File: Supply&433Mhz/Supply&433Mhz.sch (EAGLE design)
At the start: 15 parts, among them K1 61004021821, P1 DF11-06-2DSA, Q1 BS170

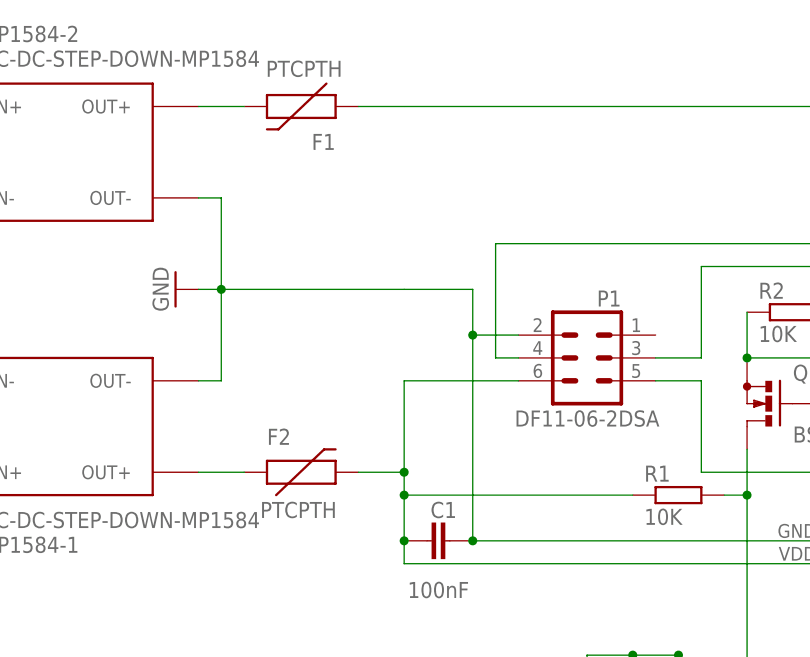
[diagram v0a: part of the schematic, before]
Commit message: Revert "Remove Schottky - Diodes, since already on DC/DC buck converter."
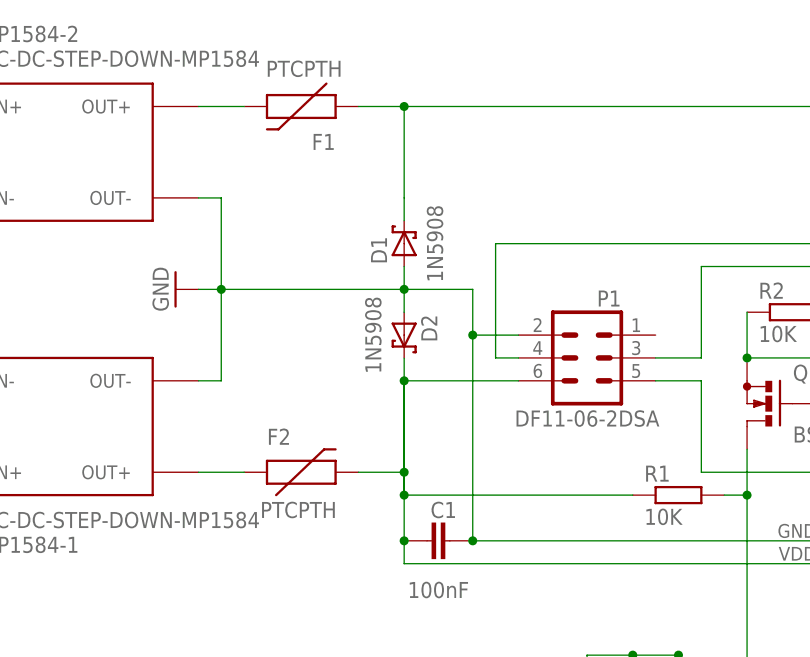
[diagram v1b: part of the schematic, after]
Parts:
- added D1, D2: 1N5908, diode:1N5908
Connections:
- net GND: now also D1.A, D2.A
- net N$2: now also D2.C
- net N$5: now also D1.C
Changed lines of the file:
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@@
 <part name="P1" library="con-hirose-df11" deviceset="DF11-06-2DSA" device=""/>
 <part name="24V" library="con-wuerth" deviceset="691131710002" device=""/>
+<part name="D1" library="diode" deviceset="1N5908" device=""/>
+<part name="D2" library="diode" deviceset="1N5908" device=""/>
 <part name="F1" library="SparkFun-PowerIC" deviceset="PTC" device="PTH"/>
 <part name="F2" library="SparkFun-PowerIC" deviceset="PTC" device="PTH"/>
@@
 </instance>
 <instance part="24V" gate="G$1" x="20.32" y="81.28" rot="MR0"/>
+<instance part="D1" gate="1" x="88.9" y="83.82" smashed="yes" rot="R90">
+<attribute name="NAME" x="86.995" y="81.534" size="1.778" layer="95" rot="R90"/>
+<attribute name="VALUE" x="91.44" y="83.82" size="1.778" layer="96" rot="R90" align="top-center"/>
+</instance>
+<instance part="D2" gate="1" x="88.9" y="73.66" smashed="yes" rot="R270">
+<attribute name="NAME" x="90.805" y="75.946" size="1.778" layer="95" rot="R270"/>
+<attribute name="VALUE" x="86.36" y="73.66" size="1.778" layer="96" rot="R270" align="top-center"/>
+</instance>
 <instance part="F1" gate="G$1" x="78.74" y="99.06" rot="R180"/>
 <instance part="F2" gate="G$1" x="76.2" y="58.42"/>
@@
 <pinref part="GND1" gate="1" pin="GND"/>
 <wire x1="66.04" y1="78.74" x2="68.58" y2="78.74" width="0.1524" layer="91"/>
+<pinref part="D2" gate="1" pin="A"/>
 <wire x1="68.58" y1="78.74" x2="88.9" y2="78.74" width="0.1524" layer="91"/>
+<wire x1="88.9" y1="78.74" x2="88.9" y2="76.2" width="0.1524" layer="91"/>
+<pinref part="D1" gate="1" pin="A"/>
+<wire x1="88.9" y1="78.74" x2="88.9" y2="81.28" width="0.1524" layer="91"/>
+<junction x="88.9" y="78.74"/>
 <wire x1="88.9" y1="78.74" x2="96.52" y2="78.74" width="0.1524" layer="91"/>
 <wire x1="96.52" y1="78.74" x2="96.52" y2="73.66" width="0.1524" layer="91"/>
@@
 <pinref part="F2" gate="G$1" pin="2"/>
 <wire x1="83.82" y1="58.42" x2="88.9" y2="58.42" width="0.1524" layer="91"/>
+<wire x1="88.9" y1="58.42" x2="88.9" y2="68.58" width="0.1524" layer="91"/>
+<pinref part="D2" gate="1" pin="C"/>
+<wire x1="88.9" y1="68.58" x2="88.9" y2="71.12" width="0.1524" layer="91"/>
 <pinref part="P1" gate="G$1" pin="6"/>
 <wire x1="101.6" y1="68.58" x2="88.9" y2="68.58" width="0.1524" layer="91"/>
+<junction x="88.9" y="68.58"/>
 <wire x1="88.9" y1="68.58" x2="88.9" y2="58.42" width="0.1524" layer="91"/>
 <pinref part="R1" gate="G$1" pin="1"/>
+<wire x1="88.9" y1="58.42" x2="88.9" y2="55.88" width="0.1524" layer="91"/>
 <wire x1="88.9" y1="55.88" x2="114.3" y2="55.88" width="0.1524" layer="91"/>
 <wire x1="88.9" y1="58.42" x2="88.9" y2="55.88" width="0.1524" layer="91"/>
@@
 <net name="N$5" class="0">
 <segment>
+<pinref part="D1" gate="1" pin="C"/>
 <pinref part="F1" gate="G$1" pin="1"/>
 <wire x1="83.82" y1="99.06" x2="88.9" y2="99.06" width="0.1524" layer="91"/>
+<wire x1="88.9" y1="99.06" x2="88.9" y2="88.9" width="0.1524" layer="91"/>
+<wire x1="88.9" y1="88.9" x2="88.9" y2="86.36" width="0.1524" layer="91"/>
 <wire x1="88.9" y1="99.06" x2="177.8" y2="99.06" width="0.1524" layer="91"/>
+<junction x="88.9" y="99.06"/>
 <wire x1="177.8" y1="99.06" x2="193.04" y2="99.06" width="0.1524" layer="91"/>
 <wire x1="193.04" y1="99.06" x2="193.04" y2="86.36" width="0.1524" layer="91"/>

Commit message: Remove Schottky - Diodes, since already on DC/DC buck converter.
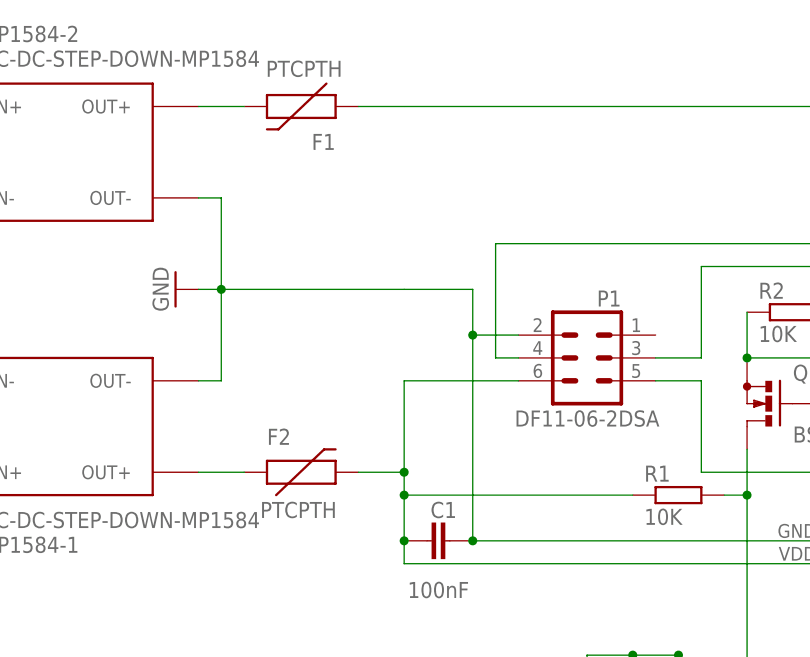
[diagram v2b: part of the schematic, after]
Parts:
- removed D1, D2: 1N5908, diode:1N5908
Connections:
- net GND: no longer D1.A, D2.A
- net N$2: no longer D2.C
- net N$5: no longer D1.C
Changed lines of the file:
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@@
 <part name="P1" library="con-hirose-df11" deviceset="DF11-06-2DSA" device=""/>
 <part name="24V" library="con-wuerth" deviceset="691131710002" device=""/>
-<part name="D1" library="diode" deviceset="1N5908" device=""/>
-<part name="D2" library="diode" deviceset="1N5908" device=""/>
 <part name="F1" library="SparkFun-PowerIC" deviceset="PTC" device="PTH"/>
 <part name="F2" library="SparkFun-PowerIC" deviceset="PTC" device="PTH"/>
@@
 </instance>
 <instance part="24V" gate="G$1" x="20.32" y="81.28" rot="MR0"/>
-<instance part="D1" gate="1" x="88.9" y="83.82" smashed="yes" rot="R90">
-<attribute name="NAME" x="86.995" y="81.534" size="1.778" layer="95" rot="R90"/>
-<attribute name="VALUE" x="91.44" y="83.82" size="1.778" layer="96" rot="R90" align="top-center"/>
-</instance>
-<instance part="D2" gate="1" x="88.9" y="73.66" smashed="yes" rot="R270">
-<attribute name="NAME" x="90.805" y="75.946" size="1.778" layer="95" rot="R270"/>
-<attribute name="VALUE" x="86.36" y="73.66" size="1.778" layer="96" rot="R270" align="top-center"/>
-</instance>
 <instance part="F1" gate="G$1" x="78.74" y="99.06" rot="R180"/>
 <instance part="F2" gate="G$1" x="76.2" y="58.42"/>
@@
 <pinref part="GND1" gate="1" pin="GND"/>
 <wire x1="66.04" y1="78.74" x2="68.58" y2="78.74" width="0.1524" layer="91"/>
-<pinref part="D2" gate="1" pin="A"/>
 <wire x1="68.58" y1="78.74" x2="88.9" y2="78.74" width="0.1524" layer="91"/>
-<wire x1="88.9" y1="78.74" x2="88.9" y2="76.2" width="0.1524" layer="91"/>
-<pinref part="D1" gate="1" pin="A"/>
-<wire x1="88.9" y1="78.74" x2="88.9" y2="81.28" width="0.1524" layer="91"/>
-<junction x="88.9" y="78.74"/>
 <wire x1="88.9" y1="78.74" x2="96.52" y2="78.74" width="0.1524" layer="91"/>
 <wire x1="96.52" y1="78.74" x2="96.52" y2="73.66" width="0.1524" layer="91"/>
@@
 <pinref part="F2" gate="G$1" pin="2"/>
 <wire x1="83.82" y1="58.42" x2="88.9" y2="58.42" width="0.1524" layer="91"/>
-<wire x1="88.9" y1="58.42" x2="88.9" y2="68.58" width="0.1524" layer="91"/>
-<pinref part="D2" gate="1" pin="C"/>
-<wire x1="88.9" y1="68.58" x2="88.9" y2="71.12" width="0.1524" layer="91"/>
 <pinref part="P1" gate="G$1" pin="6"/>
 <wire x1="101.6" y1="68.58" x2="88.9" y2="68.58" width="0.1524" layer="91"/>
-<junction x="88.9" y="68.58"/>
 <wire x1="88.9" y1="68.58" x2="88.9" y2="58.42" width="0.1524" layer="91"/>
 <pinref part="R1" gate="G$1" pin="1"/>
-<wire x1="88.9" y1="58.42" x2="88.9" y2="55.88" width="0.1524" layer="91"/>
 <wire x1="88.9" y1="55.88" x2="114.3" y2="55.88" width="0.1524" layer="91"/>
 <wire x1="88.9" y1="58.42" x2="88.9" y2="55.88" width="0.1524" layer="91"/>
@@
 <net name="N$5" class="0">
 <segment>
-<pinref part="D1" gate="1" pin="C"/>
 <pinref part="F1" gate="G$1" pin="1"/>
 <wire x1="83.82" y1="99.06" x2="88.9" y2="99.06" width="0.1524" layer="91"/>
-<wire x1="88.9" y1="99.06" x2="88.9" y2="88.9" width="0.1524" layer="91"/>
-<wire x1="88.9" y1="88.9" x2="88.9" y2="86.36" width="0.1524" layer="91"/>
 <wire x1="88.9" y1="99.06" x2="177.8" y2="99.06" width="0.1524" layer="91"/>
-<junction x="88.9" y="99.06"/>
 <wire x1="177.8" y1="99.06" x2="193.04" y2="99.06" width="0.1524" layer="91"/>
 <wire x1="193.04" y1="99.06" x2="193.04" y2="86.36" width="0.1524" layer="91"/>
